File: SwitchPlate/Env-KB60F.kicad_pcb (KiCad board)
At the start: 2 copper layers, 283 x 126.5 mm, 0 parts

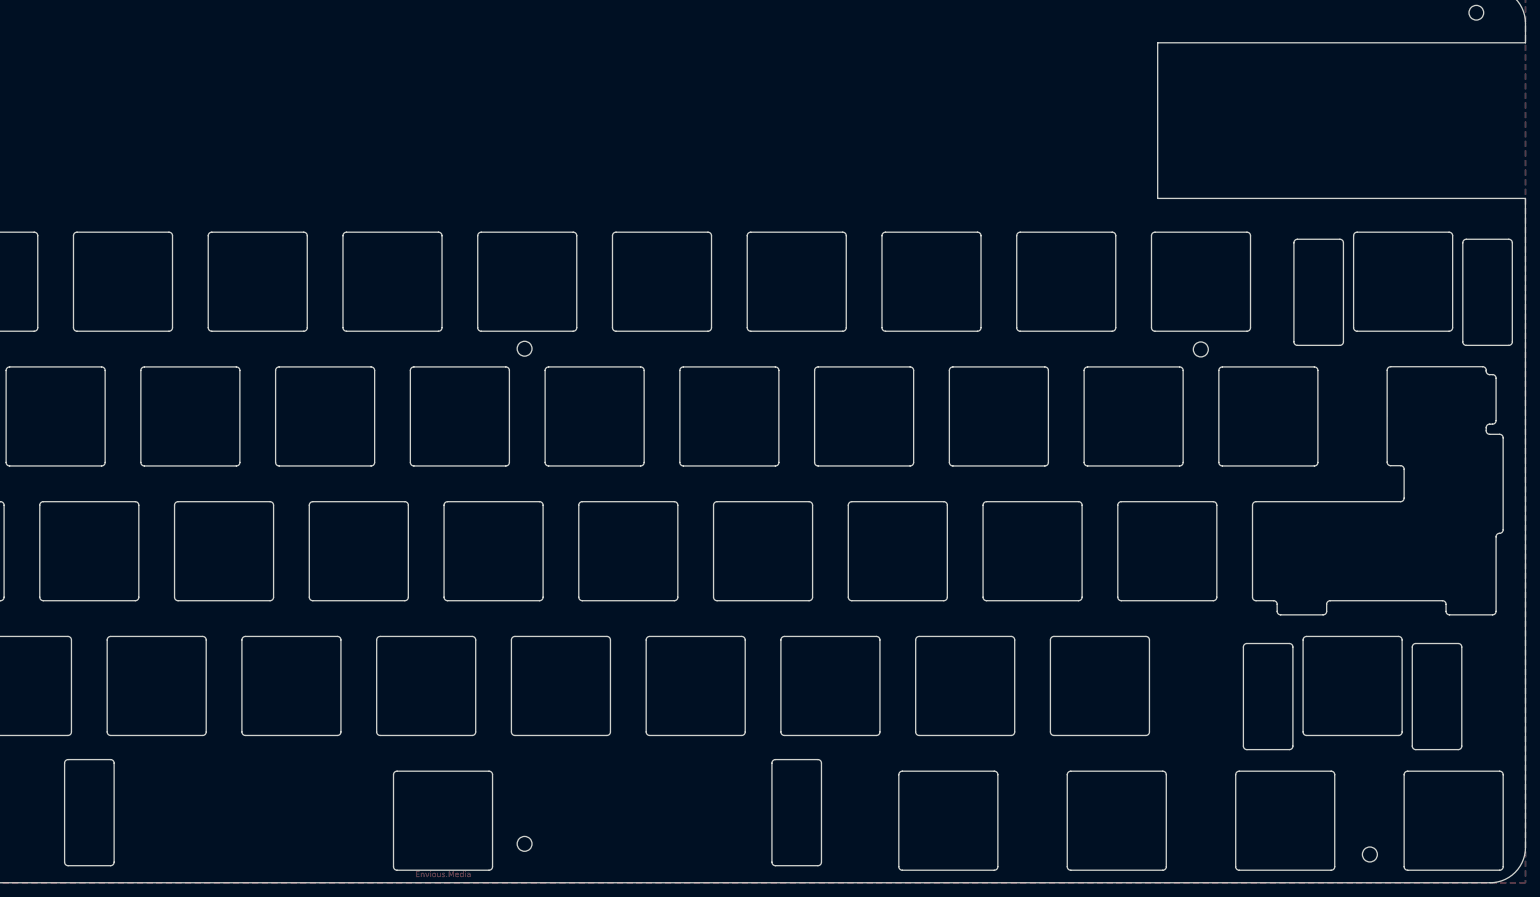
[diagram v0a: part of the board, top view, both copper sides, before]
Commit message: Corrected mount hole placement on all PCBs and updated the switch plate to fit triple spacebar split.
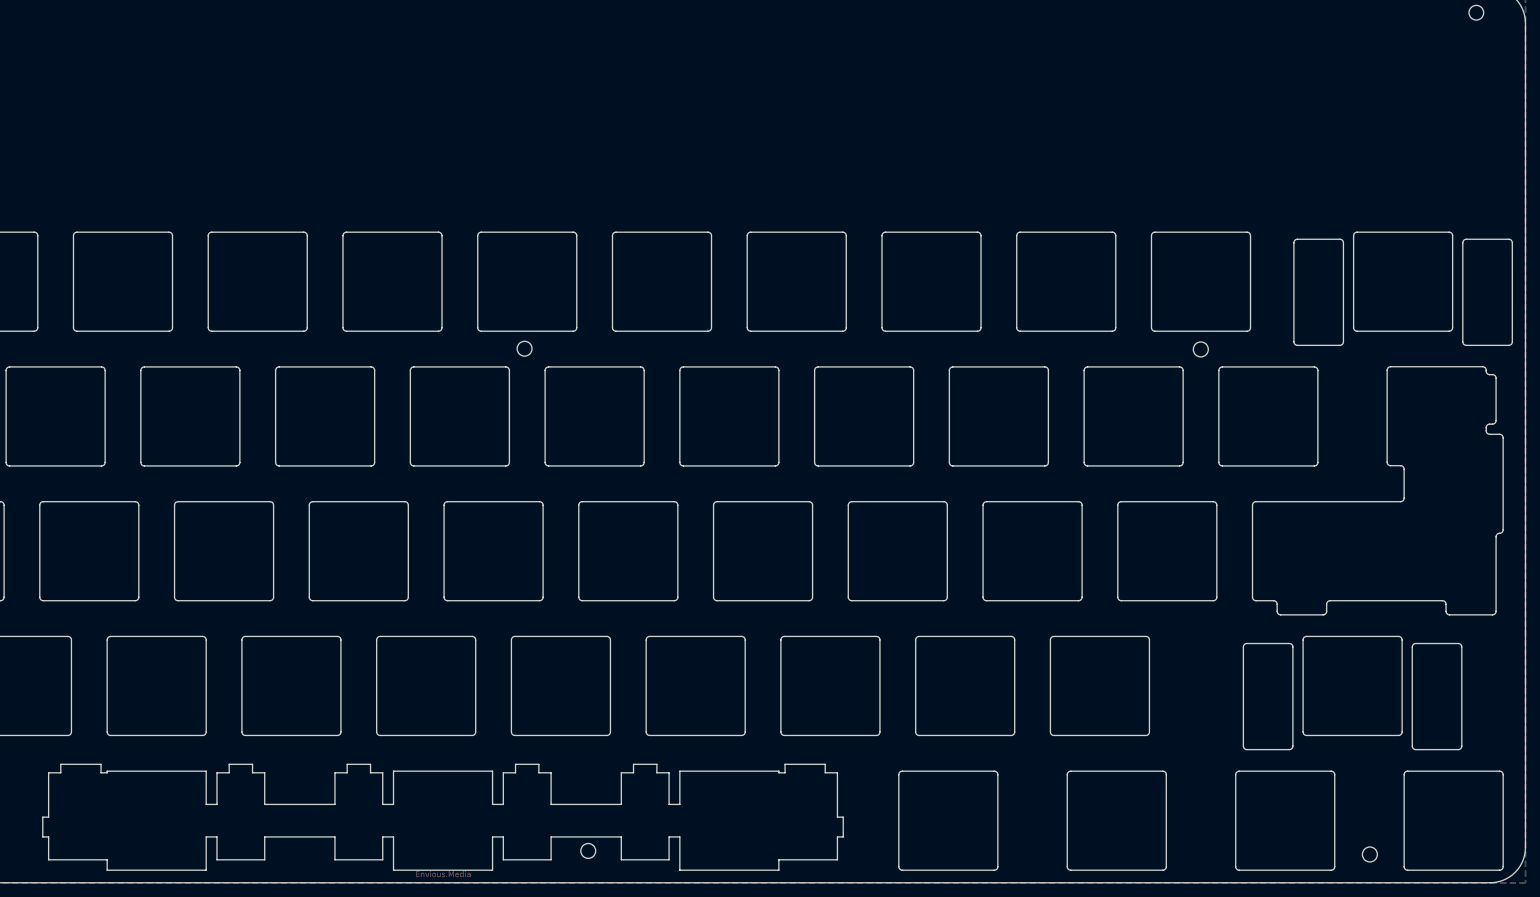
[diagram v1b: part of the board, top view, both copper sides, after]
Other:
- outline, holes or cut-outs redrawn
